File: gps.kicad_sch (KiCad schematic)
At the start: 0 parts

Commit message: Routage complet
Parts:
- added C18, C22: 10µ, Capacitor_SMD:C_0805_2012Metric, symbol Device:C
- added C19, C23, C30: 100n, Capacitor_SMD:C_0805_2012Metric, symbol Device:C
- added C20, C21: 33p, Capacitor_SMD:C_0805_2012Metric, symbol Device:C
- added C26, C27: NC, Capacitor_SMD:C_0805_2012Metric, symbol Device:C
- added C28, C29: 100p, Capacitor_SMD:C_0805_2012Metric, symbol Device:C
- added J3: 73412-0110, Connector_Coaxial:U.FL_Molex_MCRF_73412-0110_Vertical, symbol Connector:Conn_Coaxial
- added L2: 68nH, Inductor_SMD:L_0805_2012Metric, symbol Device:L_Iron_Small
- added R7: R, Resistor_SMD:R_0805_2012Metric, symbol Device:R
- added U6: LC76GPAMD, Local:XCVR_LC76G, symbol LC76G:LC76G
- added U7: AP22804AW5, Package_TO_SOT_SMD:SOT-23-5, symbol Power_Management:AP22804AW5
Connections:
- new net: C28.1, J3.1 (In), L2.1
- new net: C29.1, C30.1, L2.2, U7.1 (OUT)
- new net: C27.1, C28.2, R7.1
- new net: C26.1, R7.2, U6.11 (RF_IN)
- new net: U6.13 (ANT_ON), U7.4 (EN)
- new net: U6.14 (VDD_RF), U7.5 (IN)
- new net: U6.15 (RESERVED), U6.18 (RESERVED), U6.19 (RESERVED), U6.7 (RESERVED)
- new net +3.3V: C18.1, C19.1, C20.1, C21.1, C22.1, C23.1, U6.6 (V_BCKP), U6.8 (VCC)
- new net GND: C18.2, C19.2, C20.2, C21.2, C22.2, C23.2, C26.2, C27.2, C29.2, C30.2, J3.2 (Ext), U6.1 (GND), U6.10 (GND), U6.12 (GND), U6.28 (GND), U7.2 (GND)
- new net GPS_FIX: U6.23 (3D_FIX)
- new net GPS_JAM: U6.22 (JAM_IND)
- new net GPS_PP1: U6.4 (1PPS)
- new net GPS_REF: U6.21 (GEOFENCE)
- new net GPS_REQ: U6.5 (~{AP_REQ})
- new net GPS_RST: U6.9 (~{RESET})
- new net GPS_RX: U6.3 (RXD)
- new net GPS_SEL: U6.24 (D_SEL)
- new net GPS_TX: U6.2 (TXD)
- new net SCL: U6.17 (I2C_SCL)
- new net SDA: U6.16 (I2C_SDA)
- no-connect marks 0 -> 5

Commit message: Set MPN
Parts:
- C18, C22: JLCPCB Part # (none) -> CL21B106KPQNNNE; manf# CC1206KKX7R7BB105 -> CL21B106KPQNNNE
- C19, C23, C30: JLCPCB Part # (none) -> CL21B104KBCNNNC; manf# CC1206KKX7R7BB105 -> CL21B104KBCNNNC
- C20, C21: JLCPCB Part # (none) -> CC0805JRNPO9BN330; manf# CC1206KKX7R7BB105 -> CC0805JRNPO9BN330
- C26, C27: manf# CC1206KKX7R7BB105 -> (none)
- C28, C29: JLCPCB Part # (none) -> GRM2165C1H101JA01D; manf# CC1206KKX7R7BB105 -> GRM2165C1H101JA01D
- J3: JLCPCB Part # (none) -> 73412-0110; manf# (none) -> 73412-0110
- L2: JLCPCB Part # (none) -> MLF2012D68NMTD25; manf# (none) -> MLF2012D68NMTD25
- R7: value R -> 0; JLCPCB Part # (none) -> RC0805JR-7W0RL; manf# (none) -> RC0805JR-7W0RL
- U6: JLCPCB Part # (none) -> LC76GPAMD; manf# (none) -> LC76GPAMD
- U7: value AP22804AW5 -> AP22804AW5-7; JLCPCB Part # (none) -> AP22804AW5-7; manf# (none) -> AP22804AW5-7
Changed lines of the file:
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@@
+			)
+		)
+		(property "manf#" "73412-0110"
+			(at 33.02 64.77 90)
+			(effects
+				(font
+					(size 1.27 1.27)
+				)
+				(hide yes)
+			)
+		)
+		(property "JLCPCB Part #" "73412-0110"
+			(at 33.02 64.77 90)
+			(effects
+				(font
+					(size 1.27 1.27)
+				)
+				(hide yes)
 			)
 		)
@@
 			)
 		)
-		(property "manf#" " CC1206KKX7R7BB105"
+		(property "manf#" "GRM2165C1H101JA01D"
 			(at 45.72 106.68 0)
 			(effects
@@
 			)
 		)
+		(property "JLCPCB Part #" "GRM2165C1H101JA01D"
+			(at 45.72 106.68 0)
+			(effects
+				(font
+					(size 1.27 1.27)
+				)
+				(hide yes)
+			)
+		)
 		(pin "2"
 		)
@@
 			)
 		)
-		(property "manf#" " CC1206KKX7R7BB105"
+		(property "manf#" "CL21B104KBCNNNC"
 			(at 269.24 60.96 0)
 			(effects
@@
 			)
 		)
+		(property "JLCPCB Part #" "CL21B104KBCNNNC"
+			(at 269.24 60.96 0)
+			(effects
+				(font
+					(size 1.27 1.27)
+				)
+				(hide yes)
+			)
+		)
 		(pin "2"
 		)
@@
 			)
 		)
-		(property "Value" "R"
+		(property "Value" "0"
 			(at 68.58 69.85 90)
 			(effects
@@
 			)
 		)
+		(property "JLCPCB Part #" "RC0805JR-7W0RL"
+			(at 68.58 73.66 90)
+			(effects
+				(font
+					(size 1.27 1.27)
+				)
+				(hide yes)
+			)
+		)
+		(property "manf#" "RC0805JR-7W0RL"
+			(at 68.58 73.66 90)
+			(effects
+				(font
+					(size 1.27 1.27)
+				)
+				(hide yes)
+			)
+		)
 		(pin "1"
 		)
@@
 			)
 		)
-		(property "manf#" " CC1206KKX7R7BB105"
+		(property "manf#" "CC0805JRNPO9BN330"
 			(at 214.63 76.2 0)
 			(effects
@@
 			)
 		)
+		(property "JLCPCB Part #" "CC0805JRNPO9BN330"
+			(at 214.63 76.2 0)
+			(effects
+				(font
+					(size 1.27 1.27)
+				)
+				(hide yes)
+			)
+		)
 		(pin "2"
 		)
@@
 			)
 		)
-		(property "manf#" " CC1206KKX7R7BB105"
+		(property "manf#" "CL21B106KPQNNNE"
 			(at 257.81 60.96 0)
 			(effects
@@
 			)
 		)
+		(property "JLCPCB Part #" "CL21B106KPQNNNE"
+			(at 257.81 60.96 0)
+			(effects
+				(font
+					(size 1.27 1.27)
+				)
+				(hide yes)
+			)
+		)
 		(pin "2"
 		)
@@
 			)
 		)
-		(property "manf#" " CC1206KKX7R7BB105"
+		(property "manf#" "CL21B104KBCNNNC"
 			(at 237.49 76.2 0)
 			(effects
@@
 			)
 		)
+		(property "JLCPCB Part #" "CL21B104KBCNNNC"
+			(at 237.49 76.2 0)
+			(effects
+				(font
+					(size 1.27 1.27)
+				)
+				(hide yes)
+			)
+		)
 		(pin "2"
 		)
@@
 			)
 		)
-		(property "manf#" " CC1206KKX7R7BB105"
+		(property "manf#" "CC0805JRNPO9BN330"
 			(at 246.38 60.96 0)
 			(effects
@@
 			)
 		)
+		(property "JLCPCB Part #" "CC0805JRNPO9BN330"
+			(at 246.38 60.96 0)
+			(effects
+				(font
+					(size 1.27 1.27)
+				)
+				(hide yes)
+			)
+		)
 		(pin "2"
 		)
@@
 			)
 		)
-		(property "manf#" " CC1206KKX7R7BB105"
+		(property "manf#" ""
 			(at 57.15 80.01 0)
 			(effects
@@
 		)
 		(property "gp" " CC1206KKX7R7BB105"
+			(at 57.15 80.01 0)
+			(effects
+				(font
+					(size 1.27 1.27)
+				)
+				(hide yes)
+			)
+		)
+		(property "JLCPCB Part #" ""
 			(at 57.15 80.01 0)
 			(effects
@@
 			)
 		)
-		(property "Value" "AP22804AW5"
+		(property "Value" "AP22804AW5-7"
 			(at 87.63 95.25 0)
 			(effects
@@
 			)
 		)
+		(property "JLCPCB Part #" "AP22804AW5-7"
+			(at 87.63 102.87 0)
+			(effects
+				(font
+					(size 1.27 1.27)
+				)
+				(hide yes)
+			)
+		)
+		(property "manf#" "AP22804AW5-7"
+			(at 87.63 102.87 0)
+			(effects
+				(font
+					(size 1.27 1.27)
+				)
+				(hide yes)
+			)
+		)
 		(pin "2"
 		)
@@
 			)
 		)
-		(property "manf#" " CC1206KKX7R7BB105"
+		(property "manf#" "CL21B106KPQNNNE"
 			(at 226.06 76.2 0)
 			(effects
@@
 			)
 		)
+		(property "JLCPCB Part #" "CL21B106KPQNNNE"
+			(at 226.06 76.2 0)
+			(effects
+				(font
+					(size 1.27 1.27)
+				)
+				(hide yes)
+			)
+		)
 		(pin "2"
 		)
@@
 			)
 		)
+		(property "JLCPCB Part #" "MLF2012D68NMTD25"
+			(at 33.02 87.63 0)
+			(effects
+				(font
+					(size 1.27 1.27)
+				)
+				(hide yes)
+			)
+		)
+		(property "manf#" "MLF2012D68NMTD25"
+			(at 33.02 87.63 0)
+			(effects
+				(font
+					(size 1.27 1.27)
+				)
+				(hide yes)
+			)
+		)
 		(pin "1"
 		)
@@
 			)
 		)
-		(property "manf#" " CC1206KKX7R7BB105"
+		(property "manf#" "CL21B104KBCNNNC"
 			(at 67.31 106.68 0)
 			(effects
@@
 			)
 		)
+		(property "JLCPCB Part #" "CL21B104KBCNNNC"
+			(at 67.31 106.68 0)
+			(effects
+				(font
+					(size 1.27 1.27)
+				)
+				(hide yes)
+			)
+		)
 		(pin "2"
 		)
@@
 			)
 		)
-		(property "manf#" " CC1206KKX7R7BB105"
+		(property "manf#" ""
 			(at 78.74 80.01 0)
 			(effects
@@
 			)
 		)
+		(property "JLCPCB Part #" ""
+			(at 78.74 80.01 0)
+			(effects
+				(font
+					(size 1.27 1.27)
+				)
+				(hide yes)
+			)
+		)
 		(pin "2"
 		)
@@
 			)
 		)
-		(property "manf#" " CC1206KKX7R7BB105"
+		(property "manf#" "GRM2165C1H101JA01D"
 			(at 45.72 73.66 0)
 			(effects
@@
 			)
 		)
+		(property "JLCPCB Part #" "GRM2165C1H101JA01D"
+			(at 45.72 73.66 90)
+			(effects
+				(font
+					(size 1.27 1.27)
+				)
+				(hide yes)
+			)
+		)
 		(pin "2"
 		)
@@
 				(hide yes)
 			)
+		)
+		(property "JLCPCB Part #" "LC76GPAMD"
+			(at 143.51 78.74 0)
+			(effects
+				(font
+					(size 1.27 1.27)
+				)
+				(hide yes)
+			)
+		)
+		(property "manf#" "LC76GPAMD"
+			(at 143.51 78.74 0)
+			(effects
+				(font
+					(size 1.27 1.27)
+				)
+				(hide yes)
+			)

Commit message: Change Code for JLC part
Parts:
- C18, C22: JLCPCB Part # CL21B106KPQNNNE -> C32635
- C19, C23, C30: JLCPCB Part # CL21B104KBCNNNC -> C1711
- C20, C21: JLCPCB Part # CC0805JRNPO9BN330 -> C107115
- C28, C29: JLCPCB Part # GRM2165C1H101JA01D -> C77059
- J3: JLCPCB Part # 73412-0110 -> C434806
- L2: JLCPCB Part # MLF2012D68NMTD25 -> C404449
- R7: JLCPCB Part # RC0805JR-7W0RL -> C2936632
- U6: JLCPCB Part # LC76GPAMD -> C20607017
- U7: JLCPCB Part # AP22804AW5-7 -> C3001659
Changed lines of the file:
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@@
 			)
 		)
-		(property "JLCPCB Part #" "73412-0110"
+		(property "JLCPCB Part #" "C434806"
 			(at 33.02 64.77 90)
 			(effects
@@
 			)
 		)
-		(property "JLCPCB Part #" "GRM2165C1H101JA01D"
+		(property "JLCPCB Part #" "C77059"
 			(at 45.72 106.68 0)
 			(effects
@@
 			)
 		)
-		(property "JLCPCB Part #" "CL21B104KBCNNNC"
+		(property "JLCPCB Part #" "C1711"
 			(at 269.24 60.96 0)
 			(effects
@@
 			)
 		)
-		(property "JLCPCB Part #" "RC0805JR-7W0RL"
+		(property "JLCPCB Part #" "C2936632"
 			(at 68.58 73.66 90)
 			(effects
@@
 			)
 		)
-		(property "JLCPCB Part #" "CC0805JRNPO9BN330"
+		(property "JLCPCB Part #" "C107115"
 			(at 214.63 76.2 0)
 			(effects
@@
 			)
 		)
-		(property "JLCPCB Part #" "CL21B106KPQNNNE"
+		(property "JLCPCB Part #" "C32635"
 			(at 257.81 60.96 0)
 			(effects
@@
 			)
 		)
-		(property "JLCPCB Part #" "CL21B104KBCNNNC"
+		(property "JLCPCB Part #" "C1711"
 			(at 237.49 76.2 0)
 			(effects
@@
 			)
 		)
-		(property "JLCPCB Part #" "CC0805JRNPO9BN330"
+		(property "JLCPCB Part #" "C107115"
 			(at 246.38 60.96 0)
 			(effects
@@
 			)
 		)
-		(property "JLCPCB Part #" "AP22804AW5-7"
+		(property "JLCPCB Part #" "C3001659"
 			(at 87.63 102.87 0)
 			(effects
@@
 			)
 		)
-		(property "JLCPCB Part #" "CL21B106KPQNNNE"
+		(property "JLCPCB Part #" "C32635"
 			(at 226.06 76.2 0)
 			(effects
@@
 			)
 		)
-		(property "JLCPCB Part #" "MLF2012D68NMTD25"
+		(property "JLCPCB Part #" "C404449"
 			(at 33.02 87.63 0)
 			(effects
@@
 			)
 		)
-		(property "JLCPCB Part #" "CL21B104KBCNNNC"
+		(property "JLCPCB Part #" "C1711"
 			(at 67.31 106.68 0)
 			(effects
@@
 			)
 		)
-		(property "JLCPCB Part #" "GRM2165C1H101JA01D"
+		(property "JLCPCB Part #" "C77059"
 			(at 45.72 73.66 90)
 			(effects
@@
 			)
 		)
-		(property "JLCPCB Part #" "LC76GPAMD"
+		(property "JLCPCB Part #" "C20607017"
 			(at 143.51 78.74 0)
 			(effects

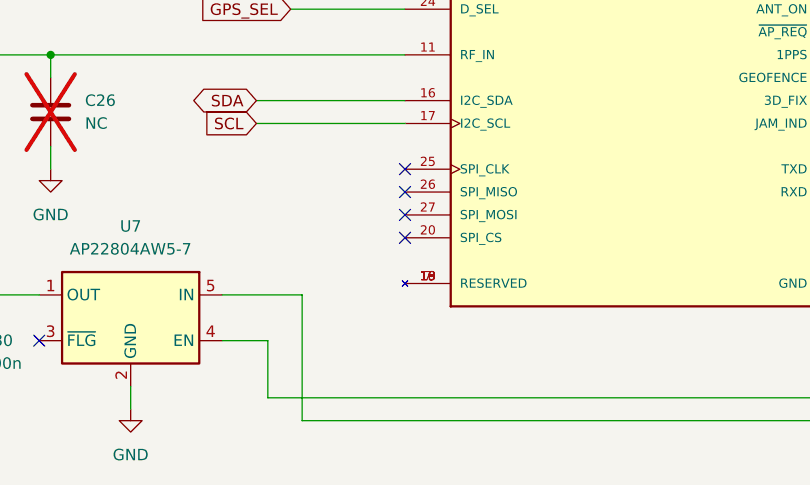
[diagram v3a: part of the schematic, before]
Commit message: Add Flash device
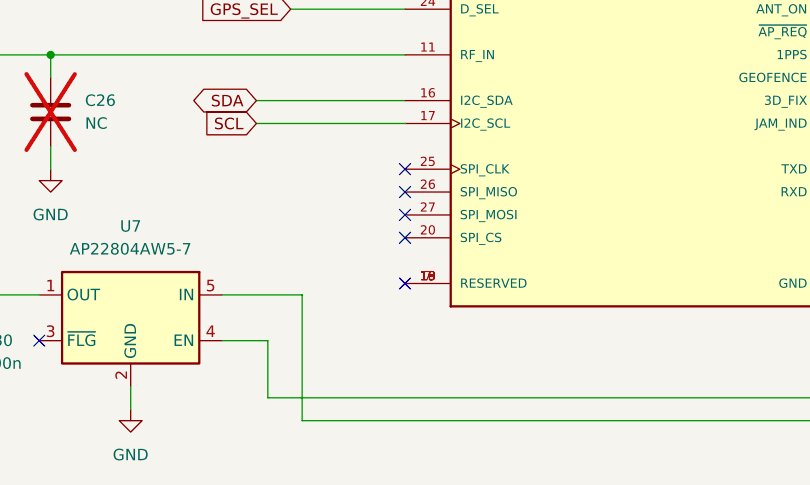
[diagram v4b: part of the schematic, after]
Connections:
- no-connect marks 5 -> 6
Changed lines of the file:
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@@
+	)
+	(no_connect
+		(at 118.11 99.06)
 	)
 	(no_connect

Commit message: Add version
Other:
- company: (none) -> Philippe12
- title: (none) -> HorseSense
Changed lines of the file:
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@@
 	(generator_version "9.0")
 	(paper "A4")
+	(title_block
+		(title "HorseSense")
+		(date "2025-11-01")
+		(rev "1.0")
+		(company "Philippe12")
+	)
 	(junction
 		(at 67.31 100.33)

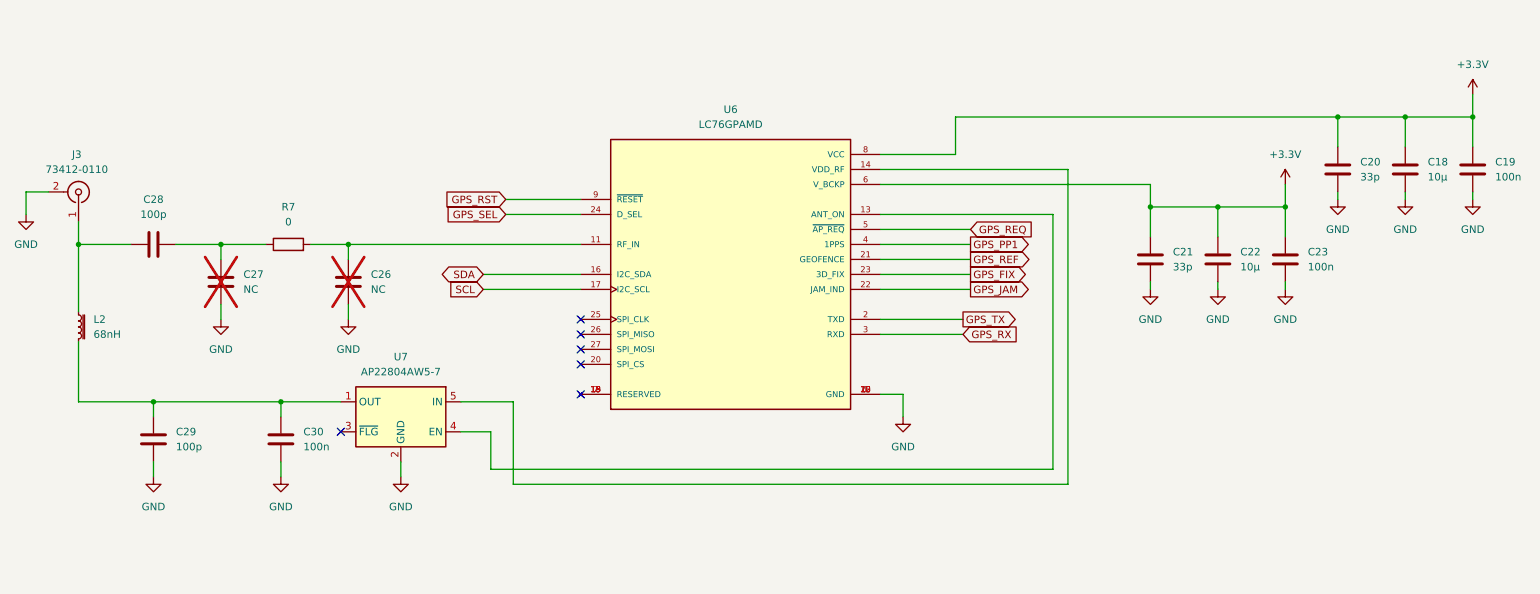
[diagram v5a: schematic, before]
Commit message: Change GNSS device
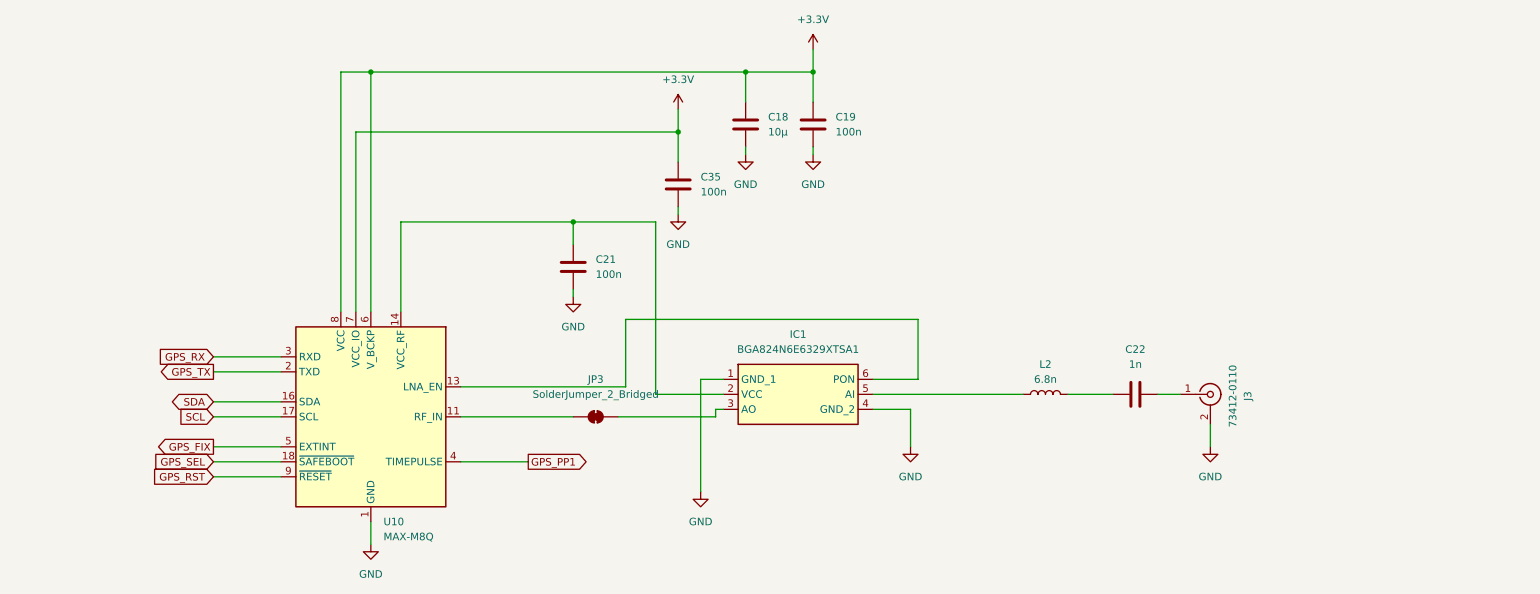
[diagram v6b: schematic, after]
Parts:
- removed C20: 33p, Capacitor_SMD:C_0805_2012Metric, symbol Device:C
- removed C23, C30: 100n, Capacitor_SMD:C_0805_2012Metric, symbol Device:C
- removed C26, C27: NC, Capacitor_SMD:C_0805_2012Metric, symbol Device:C
- removed C28, C29: 100p, Capacitor_SMD:C_0805_2012Metric, symbol Device:C
- removed L2: 68nH, Inductor_SMD:L_0805_2012Metric, symbol Device:L_Iron_Small
- removed R7: 0, Resistor_SMD:R_0805_2012Metric, symbol Device:R
- removed U6: LC76GPAMD, Local:XCVR_LC76G, symbol LC76G:LC76G
- removed U7: AP22804AW5-7, Package_TO_SOT_SMD:SOT-23-5, symbol Power_Management:AP22804AW5
- added C35: 100n, Capacitor_SMD:C_0805_2012Metric, symbol Device:C
- added IC1: BGA824N6E6329XTSA1, Local:BGA824N6E6329XTSA1, symbol BGA824N6E6329XTSA1:BGA824N6E6329XTSA1
- added JP3: SolderJumper_2_Bridged, Jumper:SolderJumper-2_P1.3mm_Bridged2Bar_RoundedPad1.0x1.5mm, symbol Jumper:SolderJumper_2_Bridged
- added L2: 6.8n, Inductor_SMD:L_0805_2012Metric, symbol Device:L
- added U10: MAX-M8Q, RF_GPS:ublox_MAX, symbol RF_GPS:MAX-M8Q
- C21: value 33p -> 100n; JLCPCB Part # C107115 -> C1711; manf# CC0805JRNPO9BN330 -> CL21B104KBCNNNC
- C22: value 10µ -> 1n; JLCPCB Part # C32635 -> C46653; gp CC1206KKX7R7BB105 -> (none); manf# CL21B106KPQNNNE -> CL21B102KBCNNNC
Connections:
- net +3.3V: now also C35.1, U10.6 (V_BCKP), U10.7 (VCC_IO), U10.8 (VCC); no longer C21.1, C22.1
- net GND: now also C35.2, IC1.1 (GND_1), IC1.4 (GND_2), U10.1 (GND), U10.10 (GND), U10.12 (GND); no longer C22.2
- net GPS_FIX: now also U10.5 (EXTINT)
- net GPS_PP1: now also U10.4 (TIMEPULSE)
- net GPS_RST: now also U10.9 (~{RESET})
- net GPS_RX: now also U10.3 (RXD)
- net GPS_SEL: now also U10.18 (~{SAFEBOOT})
- net GPS_TX: now also U10.2 (TXD)
- net SCL: now also U10.17 (SCL)
- net SDA: now also U10.16 (SDA)
- net at J3.1 (In): now also C22.2
- new net: C21.1, IC1.2 (VCC), U10.14 (VCC_RF)
- new net: IC1.5 (AI), L2.1
- new net: C22.1, L2.2
- new net: JP3.1 (A), U10.11 (RF_IN)
- new net: IC1.3 (AO), JP3.2 (B)
- new net: IC1.6 (PON), U10.13 (LNA_EN)
- no-connect marks 6 -> 0
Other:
- moved on the sheet: C18, C19, J3

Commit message: some PCB correction
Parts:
- L2: JLCPCB Part # C882493 -> C701176; manf# LQG18HN6N8J00D -> LQW2BAS6N8J00L
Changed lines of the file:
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@@
-			)
-		)
-		(property "Sim.Enable" ""
-			(at 116.84 77.47 0)
-			(effects
-				(font
-					(size 1.27 1.27)
-				)
-				(hide yes)
 			)
 		)
@@
 		)
 		(property "SnapEDA_Link" ""
-			(at 224.79 99.06 90)
-			(effects
-				(font
-					(size 1.27 1.27)
-				)
-				(hide yes)
-			)
-		)
-		(property "Sim.Enable" ""
 			(at 224.79 99.06 90)
 			(effects
@@
 			)
 		)
-		(property "Sim.Enable" ""
-			(at 134.62 63.5 0)
-			(effects
-				(font
-					(size 1.27 1.27)
-				)
-				(hide yes)
-			)
-		)
 		(pin "2"
 		)
@@
 			)
 		)
-		(property "Sim.Enable" ""
-			(at 157.48 53.34 0)
-			(effects
-				(font
-					(size 1.27 1.27)
-				)
-				(hide yes)
-			)
-		)
 		(pin "2"
 		)
@@
 			)
 		)
-		(property "JLCPCB Part #" "C882493"
+		(property "JLCPCB Part #" "C701176"
 			(at 196.85 99.06 90)
 			(effects
@@
 			)
 		)
-		(property "manf#" "LQG18HN6N8J00D"
-			(at 196.85 99.06 90)
-			(effects
-				(font
-					(size 1.27 1.27)
-				)
-				(hide yes)
-			)
-		)
-		(property "Sim.Enable" ""
+		(property "manf#" "LQW2BAS6N8J00L"
 			(at 196.85 99.06 90)
 			(effects
@@
 			)
 		)
-		(property "Sim.Enable" ""
-			(at 146.05 53.34 0)
-			(effects
-				(font
-					(size 1.27 1.27)
-				)
-				(hide yes)
-			)
-		)
 		(pin "2"
 		)
@@
 			)
 		)
-		(property "Sim.Enable" ""
-			(at 120.65 102.87 0)
-			(effects
-				(font
-					(size 1.27 1.27)
-				)
-				(hide yes)
-			)
-		)
 		(pin "1"
 		)
@@
 		)
 		(property "SnapEDA_Link" ""
-			(at 212.09 99.06 90)
-			(effects
-				(font
-					(size 1.27 1.27)
-				)
-				(hide yes)
-			)
-		)
-		(property "Sim.Enable" ""
 			(at 212.09 99.06 90)
 			(effects
@@
 			)
 		)
-		(property "Sim.Enable" ""
-			(at 139.7 96.52 0)
-			(effects
-				(font
-					(size 1.27 1.27)
-				)
-				(hide yes)
-			)
-		)
 		(pin "1"
 		)
@@
 			(at 82.55 102.87 0)
 			(effects
-				(font
-					(size 1.27 1.27)
-				)
-				(hide yes)
-			)
-		)
-		(property "Sim.Enable" ""
-			(at 82.55 102.87 0)
-			(effects
